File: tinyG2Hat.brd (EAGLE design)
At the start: 101.9 x 53.3 mm, 5 parts

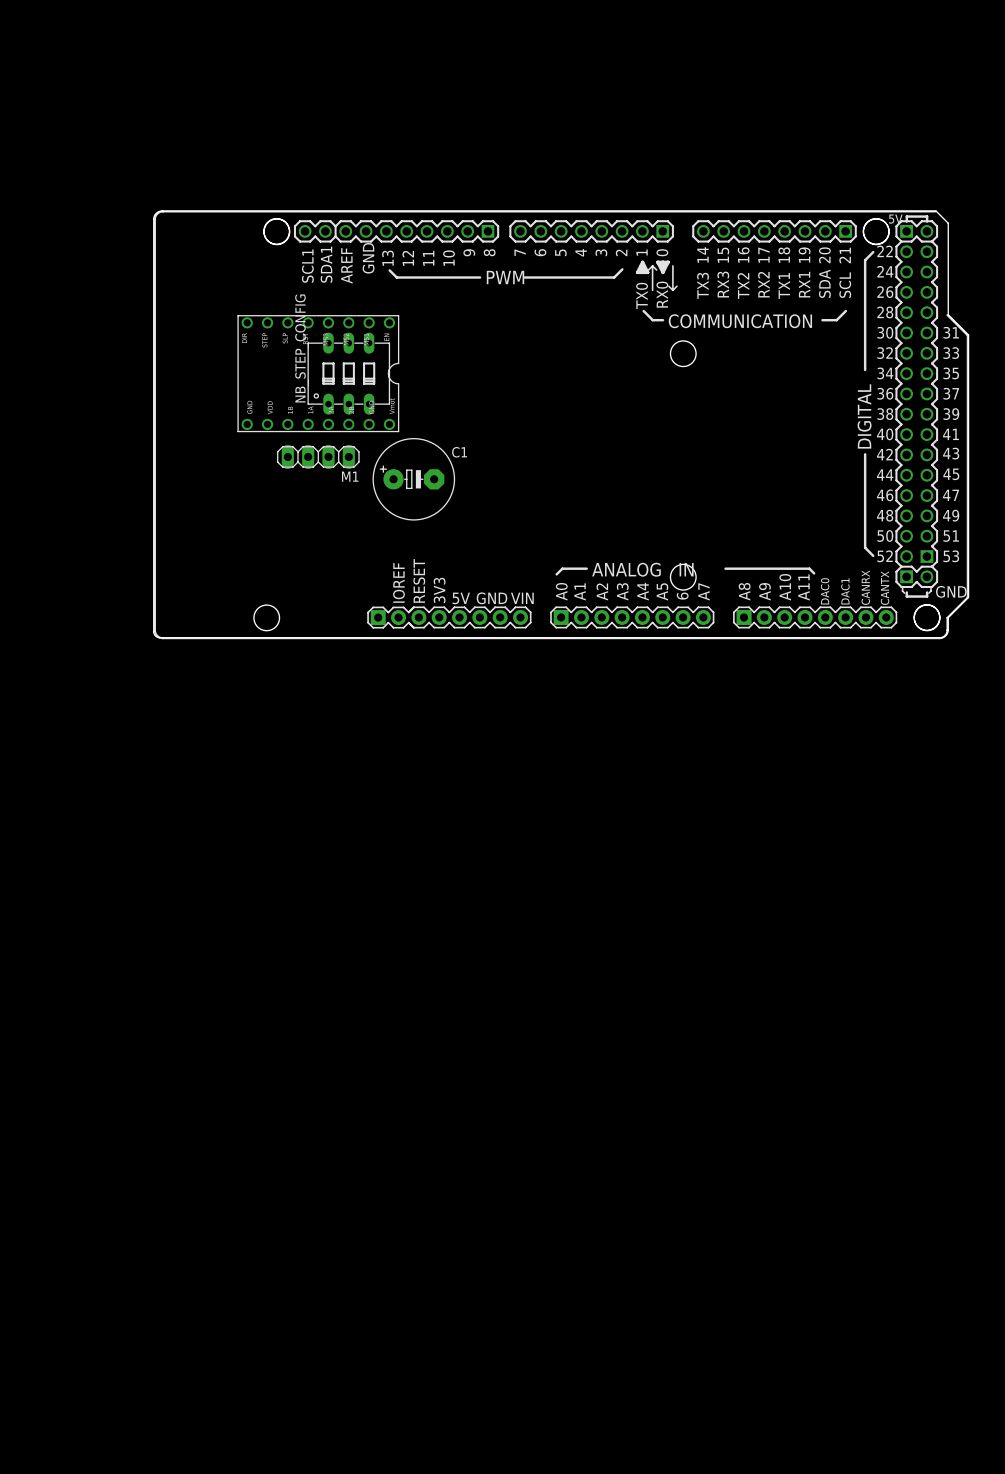
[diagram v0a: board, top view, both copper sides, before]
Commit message: 6 moteurs placés dans le schematic
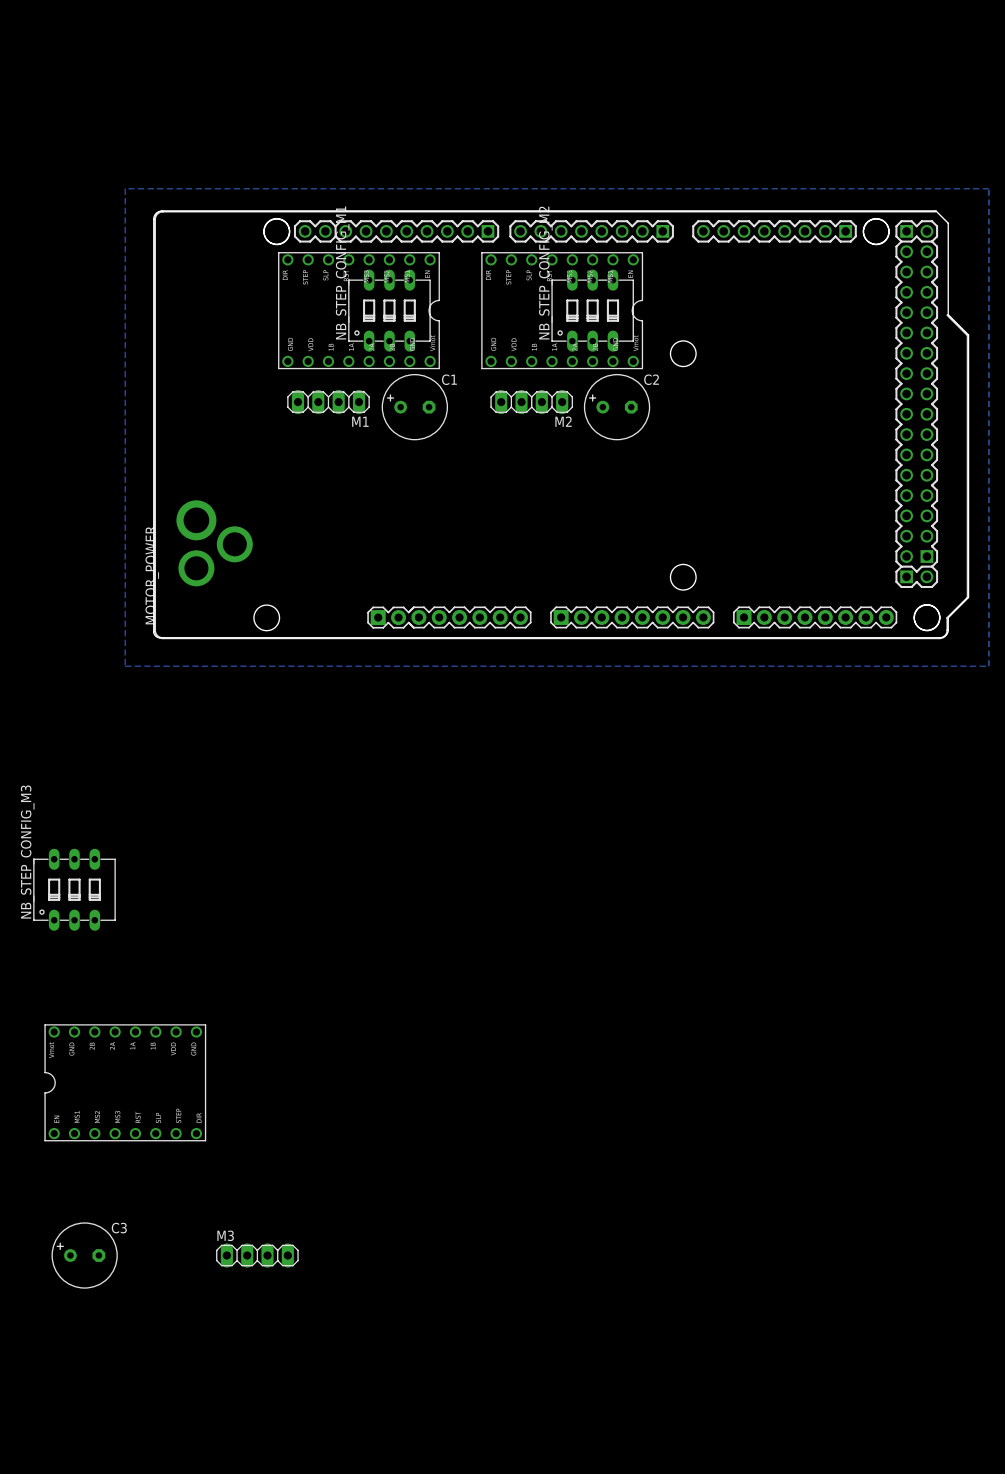
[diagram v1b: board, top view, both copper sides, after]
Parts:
- removed NB_STEP_CONFIG: (no value), switch-dil:DIP03YL
- added C2, C3: (no value), rcl:E3,5-8
- added M2, M3: (no value), pinhead:1X04
- added MOTOR_POWER: (no value), RepRapjr:RAPC712
- added NB_STEP_CONFIG_M1, NB_STEP_CONFIG_M2, NB_STEP_CONFIG_M3: (no value), switch-dil:DIP03YL
- added U$2, U$3: A4988BREAKOUT, RepRapjr:A4988BREAKOUT
- C1: device rcl:E5-10,5 -> rcl:E3,5-8
- moved U$1 9.37 mm to (33.0, 36.8)
- moved C1 9.02 mm to (32.4, 29.8)
- moved M1 6.97 mm to (21.6, 30.5)
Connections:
- new net N$10: U$2.RST, U$2.SLP
- new net N$11: M2.1, U$2.2B
- new net N$12: M2.2, U$2.2A
- new net N$13: M2.3, U$2.1A
- new net N$14: M2.4, U$2.1B
- new net N$15: NB_STEP_CONFIG_M2.6, U$2.MS3
- new net N$16: NB_STEP_CONFIG_M2.4, U$2.MS1
- new net N$17: NB_STEP_CONFIG_M3.5, U$3.MS2
- new net N$18: U$3.RST, U$3.SLP
- new net N$19: M3.1, U$3.2B
- new net N$20: M3.2, U$3.2A
- new net N$21: M3.3, U$3.1A
- new net N$22: M3.4, U$3.1B
- new net N$23: NB_STEP_CONFIG_M3.6, U$3.MS3
- new net N$24: NB_STEP_CONFIG_M3.4, U$3.MS1
- new net N$9: NB_STEP_CONFIG_M2.5, U$2.MS2
- net +24V: now also C2.+, C3.+, MOTOR_POWER.1, U$2.VMOT, U$3.VMOT
- net +3V3: now also NB_STEP_CONFIG_M1.1, NB_STEP_CONFIG_M1.2, NB_STEP_CONFIG_M1.3, NB_STEP_CONFIG_M2.1, NB_STEP_CONFIG_M2.2, NB_STEP_CONFIG_M2.3, NB_STEP_CONFIG_M3.1, NB_STEP_CONFIG_M3.2, NB_STEP_CONFIG_M3.3, U$2.VDD, U$3.VDD; no longer NB_STEP_CONFIG.1, NB_STEP_CONFIG.2, NB_STEP_CONFIG.3
- net GND: now also C2.-, C3.-, MOTOR_POWER.3, U$2.GND, U$2.GND@0, U$3.GND, U$3.GND@0
- net M2_DIR: now also U$2.DIR
- net M2_ENABLE: now also U$2.EN
- net M2_STEP: now also U$2.STEP
- net M3_DIR: now also U$3.DIR
- net M3_ENABLE: now also U$3.EN
- net M3_STEP: now also U$3.STEP
- net N$1: now also NB_STEP_CONFIG_M1.6; no longer NB_STEP_CONFIG.6
- net N$2: now also NB_STEP_CONFIG_M1.5; no longer NB_STEP_CONFIG.5
- net N$3: now also NB_STEP_CONFIG_M1.4; no longer NB_STEP_CONFIG.4
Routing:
- added copper zone on layer 16, net GND

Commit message: Ajout des entrée capteurs fin course et sortie spindle dans le schematic
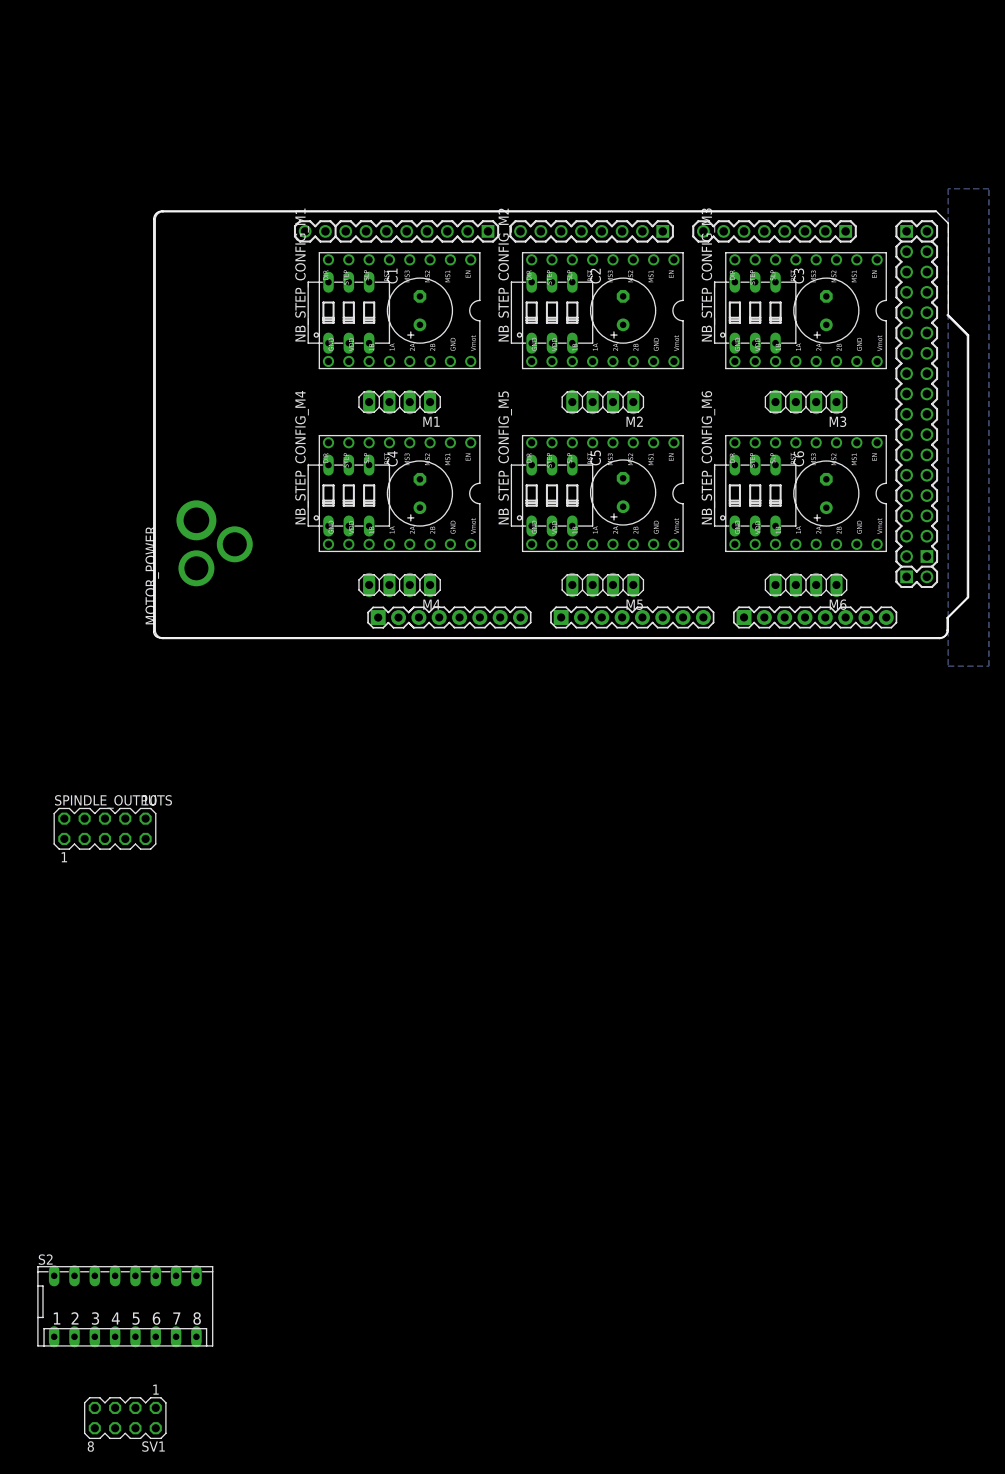
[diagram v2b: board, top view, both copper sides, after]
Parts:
- added C4, C5, C6: (no value), rcl:E3,5-8
- added M4, M5, M6: (no value), pinhead:1X04
- added NB_STEP_CONFIG_M4, NB_STEP_CONFIG_M5, NB_STEP_CONFIG_M6: (no value), switch-dil:DIP03YL
- added S2: (no value), switch-dil:DP-08
- added SPINDLE_OUTPUTS: (no value), con-lstb:MA05-2
- added SV1: (no value), con-lstb:MA04-2
- added U$4, U$5, U$6: A4988BREAKOUT, RepRapjr:A4988BREAKOUT
- moved C3 150.2 mm to (83.8, 41.9), turned to 90 degrees
- moved U$3 132.4 mm to (88.9, 36.8), turned to 180 degrees
- moved M3 126.8 mm to (81.3, 30.5), turned to 180 degrees
- moved NB_STEP_CONFIG_M3 111.6 mm to (74.9, 41.7)
- moved C2 12.1 mm to (58.4, 41.9), turned to 90 degrees
- moved C1 12.1 mm to (33.0, 41.9), turned to 90 degrees
- moved M1 8.89 mm to (30.5, 30.5)
- moved M2 8.89 mm to (55.9, 30.5)
- moved NB_STEP_CONFIG_M1 5.09 mm to (24.1, 41.7)
- moved NB_STEP_CONFIG_M2 5.09 mm to (49.5, 41.7)
- moved U$1 5.08 mm to (38.1, 36.8)
- moved U$2 5.08 mm to (63.5, 36.8)
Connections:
- new net COOLANT_ON: ARDUINO_DUE1.A3, SPINDLE_OUTPUTS.1
- new net CY_START: ARDUINO_DUE1.A2
- new net EEED_HOLD: ARDUINO_DUE1.A1
- new net E_STOP: ARDUINO_DUE1.A4, S2.10
- new net H_INTERLCK: ARDUINO_DUE1.A6, S2.9
- new net N$25: NB_STEP_CONFIG_M4.5, U$4.MS2
- new net N$26: U$4.RST, U$4.SLP
- new net N$27: M4.1, U$4.2B
- new net N$28: M4.2, U$4.2A
- new net N$29: M4.3, U$4.1A
- new net N$30: M4.4, U$4.1B
- new net N$31: NB_STEP_CONFIG_M4.6, U$4.MS3
- new net N$32: NB_STEP_CONFIG_M4.4, U$4.MS1
- new net N$33: NB_STEP_CONFIG_M5.5, U$5.MS2
- new net N$34: U$5.RST, U$5.SLP
- new net N$35: M5.1, U$5.2B
- new net N$36: M5.2, U$5.2A
- new net N$37: M5.3, U$5.1A
- new net N$38: M5.4, U$5.1B
- new net N$39: NB_STEP_CONFIG_M5.6, U$5.MS3
- new net N$40: NB_STEP_CONFIG_M5.4, U$5.MS1
- new net N$41: NB_STEP_CONFIG_M6.5, U$6.MS2
- new net N$42: U$6.RST, U$6.SLP
- new net N$43: M6.1, U$6.2B
- new net N$44: M6.2, U$6.2A
- new net N$45: M6.3, U$6.1A
- new net N$46: M6.4, U$6.1B
- new net N$47: NB_STEP_CONFIG_M6.6, U$6.MS3
- new net N$48: NB_STEP_CONFIG_M6.4, U$6.MS1
- new net N$49: S2.1, S2.2, SV1.7
- new net N$51: S2.3, S2.4, SV1.5
- new net N$53: S2.5, S2.6, SV1.3
- new net N$55: S2.7, S2.8, SV1.1
- new net SOFT_RESET: ARDUINO_DUE1.A0
- net +24V: now also C4.+, C5.+, C6.+, U$4.VMOT, U$5.VMOT, U$6.VMOT
- net +3V3: now also NB_STEP_CONFIG_M4.1, NB_STEP_CONFIG_M4.2, NB_STEP_CONFIG_M4.3, NB_STEP_CONFIG_M5.1, NB_STEP_CONFIG_M5.2, NB_STEP_CONFIG_M5.3, NB_STEP_CONFIG_M6.1, NB_STEP_CONFIG_M6.2, NB_STEP_CONFIG_M6.3, U$4.VDD, U$5.VDD, U$6.VDD
- net GND: now also C4.-, C5.-, C6.-, SPINDLE_OUTPUTS.10, SPINDLE_OUTPUTS.2, SPINDLE_OUTPUTS.4, SPINDLE_OUTPUTS.6, SPINDLE_OUTPUTS.8, SV1.2, SV1.4, SV1.6, SV1.8, U$4.GND, U$4.GND@0, U$5.GND, U$5.GND@0, U$6.GND, U$6.GND@0
- net M4_DIR: now also U$4.DIR
- net M4_ENABLE: now also U$4.EN
- net M4_STEP: now also U$4.STEP
- net M5_DIR: now also U$5.DIR
- net M5_ENABLE: now also U$5.EN
- net M5_STEP: now also U$5.STEP
- net M6_DIR: now also U$6.DIR
- net M6_ENABLE: now also U$6.EN
- net M6_STEP: now also U$6.STEP
- net SPINDLE_DIR: now also SPINDLE_OUTPUTS.7
- net SPINDLE_ENABLE: now also SPINDLE_OUTPUTS.9
- net SPINDLE_PWM: now also SPINDLE_OUTPUTS.5
- net SPINDLE_PWM2: now also SPINDLE_OUTPUTS.3
- net X_MAX: now also S2.15
- net X_MIN: now also S2.16
- net Y_MAX: now also S2.13
- net Y_MIN: now also S2.14
- net Z_MAX: now also S2.11
- net Z_MIN: now also S2.12

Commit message: Ajout des commandes manuelles
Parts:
- added CONTROL_SWITCHES_INPUTS: (no value), pinhead:2X05
- added RESET_SWITCH: (no value), RepRapjr:B3F-10XX-RPAD
- moved SV1 185.7 mm to (95.0, 60.7), turned to 270 degrees
- moved S2 163.9 mm to (75.4, 61.0), turned to 180 degrees
- moved SPINDLE_OUTPUTS 68.3 mm to (6.86, 44.2), turned to 90 degrees
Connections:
- removed net EEED_HOLD: ARDUINO_DUE1.A1
- new net FEED_HOLD: ARDUINO_DUE1.A1, CONTROL_SWITCHES_INPUTS.4
- new net N$50: CONTROL_SWITCHES_INPUTS.10, RESET_SWITCH.3
- net CY_START: now also CONTROL_SWITCHES_INPUTS.6
- net E_STOP: now also CONTROL_SWITCHES_INPUTS.8, S2.15; no longer S2.10
- net GND: now also CONTROL_SWITCHES_INPUTS.1, CONTROL_SWITCHES_INPUTS.3, CONTROL_SWITCHES_INPUTS.5, CONTROL_SWITCHES_INPUTS.7, CONTROL_SWITCHES_INPUTS.9, RESET_SWITCH.2, RESET_SWITCH.4
- net H_INTERLCK: now also S2.16; no longer S2.9
- net RESET: now also RESET_SWITCH.1
- net SOFT_RESET: now also CONTROL_SWITCHES_INPUTS.2
- net X_MAX: now also S2.10; no longer S2.15
- net X_MIN: now also S2.9; no longer S2.16
- net Y_MAX: now also S2.12; no longer S2.13
- net Y_MIN: now also S2.11; no longer S2.14
- net Z_MAX: now also S2.14; no longer S2.11
- net Z_MIN: now also S2.13; no longer S2.12
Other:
- board size 101.9 x 53.3 mm -> 101.9 x 68.6 mm

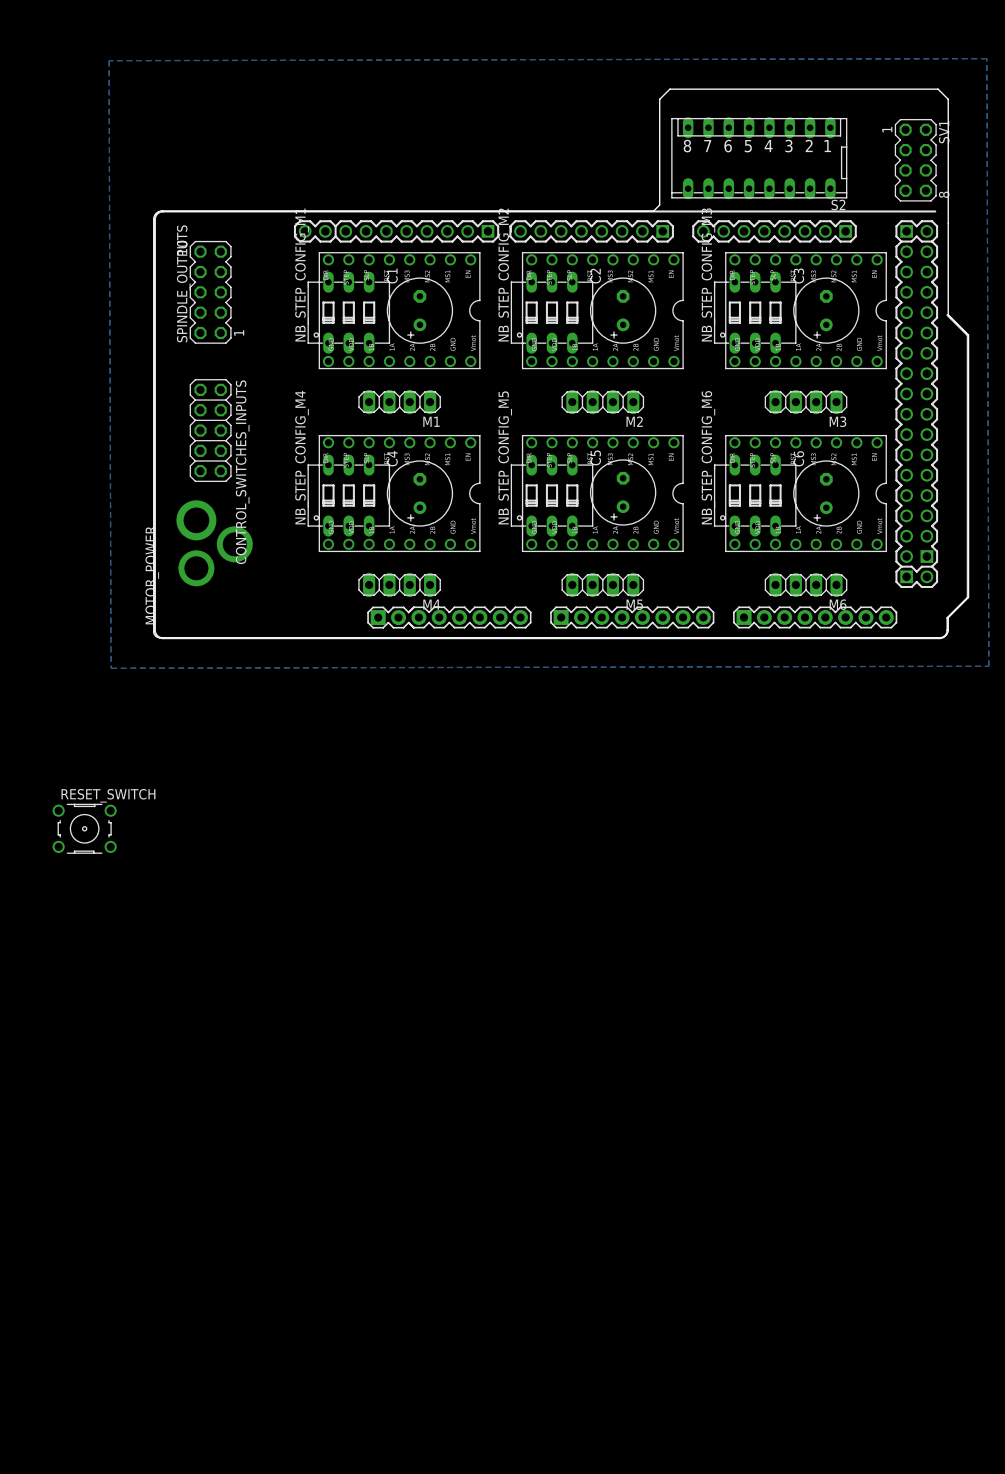
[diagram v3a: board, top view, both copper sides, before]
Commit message: Routage du Spindle, M1 et M2
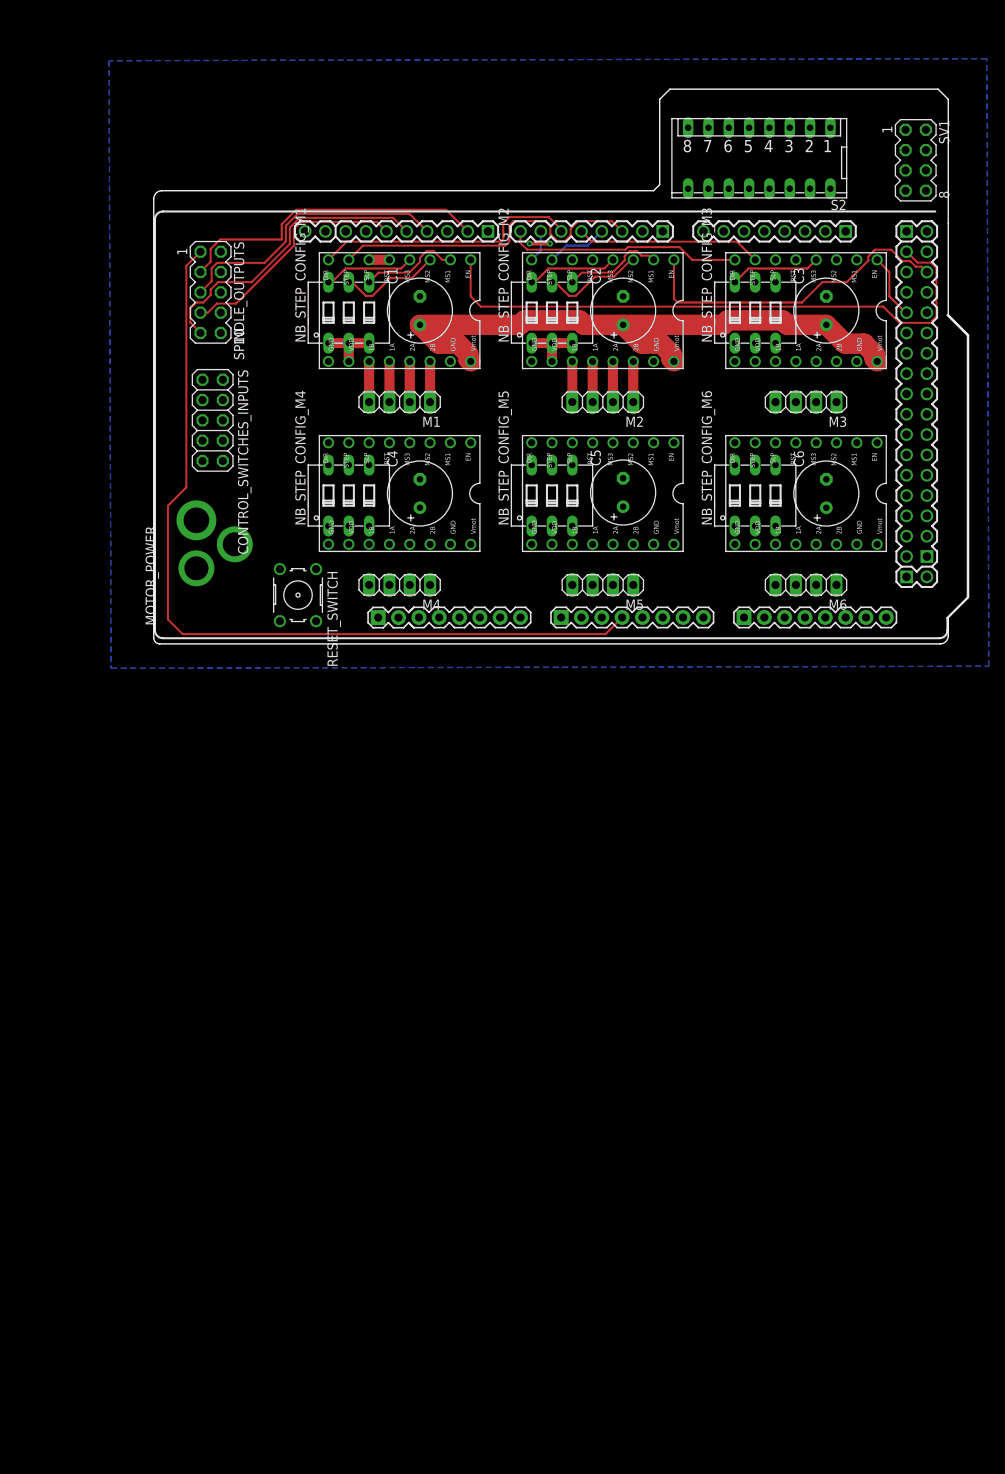
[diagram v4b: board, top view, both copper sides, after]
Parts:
- C1, C2, C3, C4, C5, C6: value (none) -> 100µF
- moved RESET_SWITCH 39.6 mm to (17.8, 6.35), turned to 270 degrees
- moved CONTROL_SWITCHES_INPUTS 1.30 mm to (7.11, 28.2)
- turned SPINDLE_OUTPUTS to 270 degrees
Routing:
- net COOLANT_ON: track 0.00 -> 106.0 mm
- net +24V: track 0.00 -> 77.5 mm
- net M1_ENABLE: track 0.00 -> 75.2 mm
- net M1_STEP: track 0.00 -> 41.0 mm
- net M2_ENABLE: track 0.00 -> 40.9 mm
- net SPINDLE_PWM2: track 0.00 -> 39.8 mm
- net SPINDLE_ENABLE: track 0.00 -> 37.7 mm
- net SPINDLE_PWM: track 0.00 -> 35.4 mm
- net M1_DIR: track 0.00 -> 33.4 mm
- net SPINDLE_DIR: track 0.00 -> 29.6 mm
- net M3_DIR: track 0.00 -> 29.4 mm
- net M3_STEP: track 0.00 -> 23.2 mm
- net +3V3: track 0.00 -> 14.7 mm
- net N$2: track 0.00 -> 12.7 mm
- net N$9: track 0.00 -> 12.7 mm
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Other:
- board size 101.9 x 68.6 mm -> 101.9 x 69.3 mm
